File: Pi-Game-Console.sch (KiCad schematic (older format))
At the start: 115 parts, among them J1 Conn_01x02_Female, J10 Conn_01x04_Female, J2 FPC_Connector, J3 Conn_Coaxial, J5 Micro_SD_Card, J6 CAM1, J7 USB_A, J8 USB_A, J9 Conn_01x04_Female, SW1 SW_DIP_x01, SW10 Y_Button, SW11 D_PAD_UP_Button, SW12 D_PAD_DOWN_Button, SW13 D_PAD_LEFT_Button, SW14 D_PAD_RIGHT_Button, SW2 Home_Button, SW3 Start_Button, SW4 Select_Button, SW5 L_Button, SW6 R_Button, SW7 A_Button, SW8 B_Button, SW9 X_Button, U2 TDA2822, U3 FAN5333BSX, U4 AR1100, U5 ATmega32U4-AU, U6 FE1.1s, Y1 12MHz, Y2 16MHz, Y3 12MHz

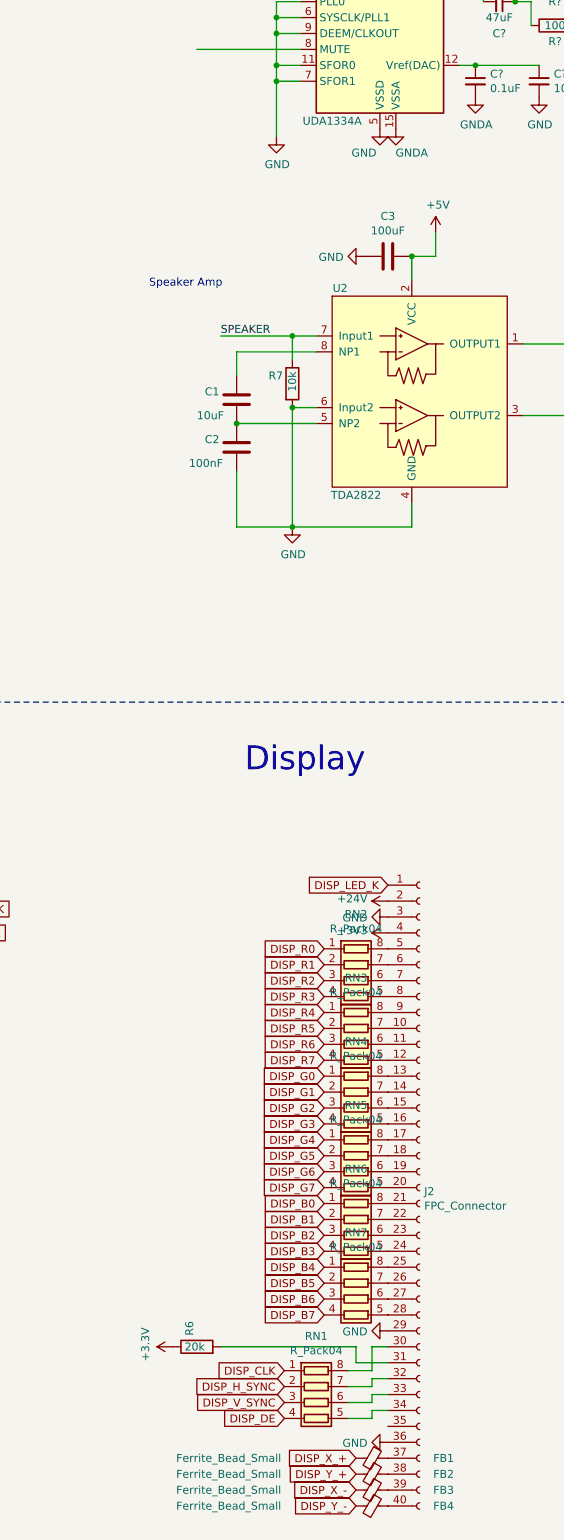
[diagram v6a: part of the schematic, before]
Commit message: Removed resistor arrays feeding into display
I really don't know that they're necessary, since the TFT friend from Adafruit doesn't have them, and they drive up the component count a fair amount.  Plus they're a real pain to solder.  If we change our mind later, they're easy to add back in.
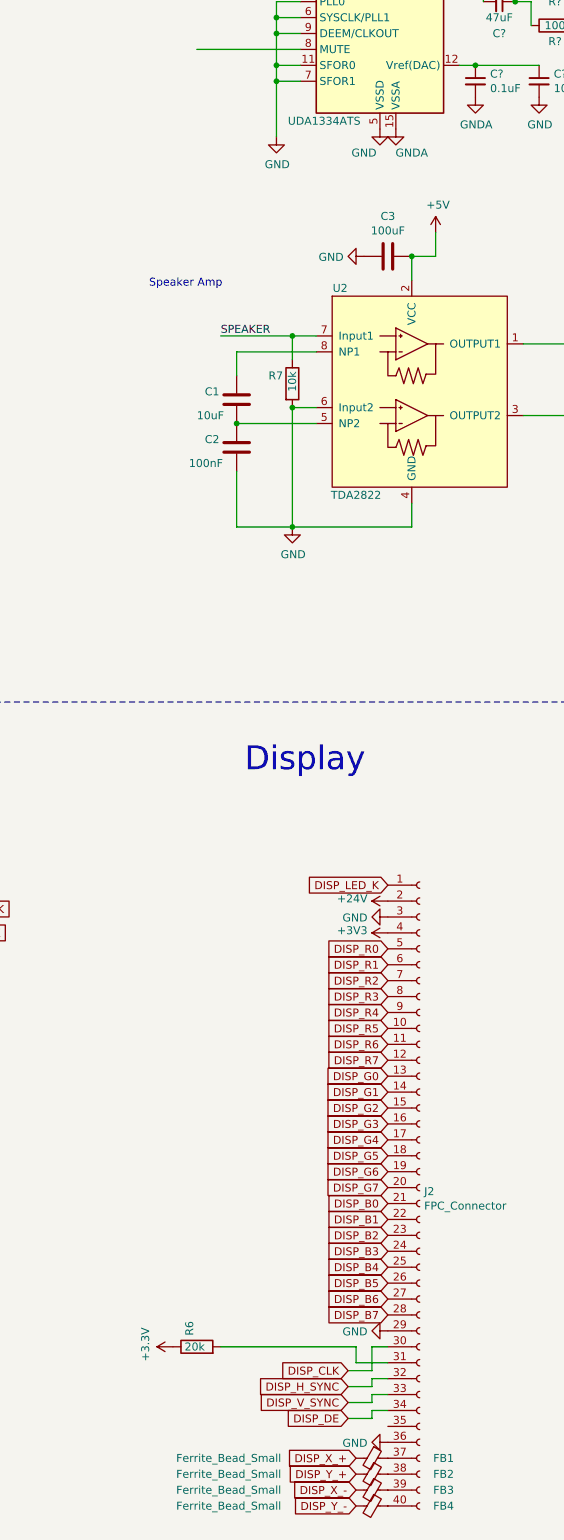
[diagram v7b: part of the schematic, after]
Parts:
- removed RN1, RN2, RN3, RN4, RN5, RN6, RN7: R_Pack04, symbol Device:R_Pack04
- U?: value UDA1334A -> UDA1334ATS
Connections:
- net DISP_B0: now also J2.21 (Pin_21)
- net DISP_B1: now also J2.22 (Pin_22)
- net DISP_B2: now also J2.23 (Pin_23)
- net DISP_B3: now also J2.24 (Pin_24)
- net DISP_B4: now also J2.25 (Pin_25)
- net DISP_B5: now also J2.26 (Pin_26)
- net DISP_B6: now also J2.27 (Pin_27)
- net DISP_B7: now also J2.28 (Pin_28)
- net DISP_CLK: now also J2.30 (Pin_30)
- net DISP_DE: now also J2.34 (Pin_34)
- net DISP_G0: now also J2.13 (Pin_13)
- net DISP_G1: now also J2.14 (Pin_14)
- net DISP_G2: now also J2.15 (Pin_15)
- net DISP_G3: now also J2.16 (Pin_16)
- net DISP_G4: now also J2.17 (Pin_17)
- net DISP_G5: now also J2.18 (Pin_18)
- net DISP_G6: now also J2.19 (Pin_19)
- net DISP_G7: now also J2.20 (Pin_20)
- net DISP_H_SYNC: now also J2.32 (Pin_32)
- net DISP_R0: now also J2.5 (Pin_5)
- net DISP_R1: now also J2.6 (Pin_6)
- net DISP_R2: now also J2.7 (Pin_7)
- net DISP_R3: now also J2.8 (Pin_8)
- net DISP_R4: now also J2.9 (Pin_9)
- net DISP_R5: now also J2.10 (Pin_10)
- net DISP_R6: now also J2.11 (Pin_11)
- net DISP_R7: now also J2.12 (Pin_12)
- net DISP_V_SYNC: now also J2.33 (Pin_33)
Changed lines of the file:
@@
 Wire Wire Line
 	20050 9150 19900 9150
-Text GLabel 6450 13350 0    50   Input ~ 0
+Text GLabel 6850 13350 0    50   Input ~ 0
 DISP_B2
-Text GLabel 6450 13450 0    50   Input ~ 0
+Text GLabel 6850 13450 0    50   Input ~ 0
 DISP_B3
-Text GLabel 6450 13550 0    50   Input ~ 0
+Text GLabel 6850 13550 0    50   Input ~ 0
 DISP_B4
-Text GLabel 6200 14300 0    50   Input ~ 0
+Text GLabel 6600 14300 0    50   Input ~ 0
 DISP_H_SYNC
-Text GLabel 6200 14400 0    50   Input ~ 0
+Text GLabel 6600 14400 0    50   Input ~ 0
 DISP_V_SYNC
-Text GLabel 6450 13650 0    50   Input ~ 0
+Text GLabel 6850 13650 0    50   Input ~ 0
 DISP_B5
-Text GLabel 6450 13750 0    50   Input ~ 0
+Text GLabel 6850 13750 0    50   Input ~ 0
 DISP_B6
-Text GLabel 6450 13850 0    50   Input ~ 0
+Text GLabel 6850 13850 0    50   Input ~ 0
 DISP_B7
-Text GLabel 6450 12750 0    50   Input ~ 0
+Text GLabel 6850 12750 0    50   Input ~ 0
 DISP_G4
-Text GLabel 6450 12850 0    50   Input ~ 0
+Text GLabel 6850 12850 0    50   Input ~ 0
 DISP_G5
-Text GLabel 6450 12950 0    50   Input ~ 0
+Text GLabel 6850 12950 0    50   Input ~ 0
 DISP_G6
-Text GLabel 6450 13050 0    50   Input ~ 0
+Text GLabel 6850 13050 0    50   Input ~ 0
 DISP_G7
-Text GLabel 6200 14200 0    50   Input ~ 0
+Text GLabel 6600 14200 0    50   Input ~ 0
 DISP_CLK
-Text GLabel 6200 14500 0    50   Input ~ 0
+Text GLabel 6600 14500 0    50   Input ~ 0
 DISP_DE
-Text GLabel 6450 13150 0    50   Input ~ 0
+Text GLabel 6850 13150 0    50   Input ~ 0
 DISP_B0
-Text GLabel 6450 13250 0    50   Input ~ 0
+Text GLabel 6850 13250 0    50   Input ~ 0
 DISP_B1
-Text GLabel 6450 12350 0    50   Input ~ 0
+Text GLabel 6850 12350 0    50   Input ~ 0
 DISP_G0
-Text GLabel 6450 11750 0    50   Input ~ 0
+Text GLabel 6850 11750 0    50   Input ~ 0
 DISP_R2
-Text GLabel 6450 11550 0    50   Input ~ 0
+Text GLabel 6850 11550 0    50   Input ~ 0
 DISP_R0
-Text GLabel 6450 11650 0    50   Input ~ 0
+Text GLabel 6850 11650 0    50   Input ~ 0
 DISP_R1
-Text GLabel 6450 11850 0    50   Input ~ 0
+Text GLabel 6850 11850 0    50   Input ~ 0
 DISP_R3
-Text GLabel 6450 11950 0    50   Input ~ 0
+Text GLabel 6850 11950 0    50   Input ~ 0
 DISP_R4
-Text GLabel 6450 12050 0    50   Input ~ 0
+Text GLabel 6850 12050 0    50   Input ~ 0
 DISP_R5
-Text GLabel 6450 12150 0    50   Input ~ 0
+Text GLabel 6850 12150 0    50   Input ~ 0
 DISP_R6
-Text GLabel 6450 12250 0    50   Input ~ 0
+Text GLabel 6850 12250 0    50   Input ~ 0
 DISP_R7
 $Comp
@@
 Wire Wire Line
 	10800 2750 10800 2450
-$Comp
-L Device:R_Pack04 RN2
-U 1 1 5E45DF44
-P 6650 11750
-F 0 "RN2" V 6233 11750 50  0000 C CNN
-F 1 "R_Pack04" V 6324 11750 50  0000 C CNN
-F 2 "" V 6925 11750 50  0001 C CNN
-F 3 "~" H 6650 11750 50  0001 C CNN
-	1    6650 11750
-	0    1    1    0
-$EndComp
-$Comp
-L Device:R_Pack04 RN3
-U 1 1 5E4602BE
-P 6650 12150
-F 0 "RN3" V 6233 12150 50  0000 C CNN
-F 1 "R_Pack04" V 6324 12150 50  0000 C CNN
-F 2 "" V 6925 12150 50  0001 C CNN
-F 3 "~" H 6650 12150 50  0001 C CNN
-	1    6650 12150
-	0    1    1    0
-$EndComp
-$Comp
-L Device:R_Pack04 RN6
-U 1 1 5E4620A6
-P 6650 13350
-F 0 "RN6" V 6233 13350 50  0000 C CNN
-F 1 "R_Pack04" V 6324 13350 50  0000 C CNN
-F 2 "" V 6925 13350 50  0001 C CNN
-F 3 "~" H 6650 13350 50  0001 C CNN
-	1    6650 13350
-	0    1    1    0
-$EndComp
-$Comp
-L Device:R_Pack04 RN7
-U 1 1 5E462A96
-P 6650 13750
-F 0 "RN7" V 6233 13750 50  0000 C CNN
-F 1 "R_Pack04" V 6324 13750 50  0000 C CNN
-F 2 "" V 6925 13750 50  0001 C CNN
-F 3 "~" H 6650 13750 50  0001 C CNN
-	1    6650 13750
-	0    1    1    0
-$EndComp
-$Comp
-L Device:R_Pack04 RN1
-U 1 1 5E4F56A2
-P 6400 14400
-F 0 "RN1" V 5983 14400 50  0000 C CNN
-F 1 "R_Pack04" V 6074 14400 50  0000 C CNN
-F 2 "" V 6675 14400 50  0001 C CNN
-F 3 "~" H 6400 14400 50  0001 C CNN
-	1    6400 14400
-	0    1    1    0
-$EndComp
 Wire Wire Line
 	6600 14300 6750 14300
@@
 	1    0    0    -1
 $EndComp
-$Comp
-L Device:R_Pack04 RN5
-U 1 1 5E4617F3
-P 6650 12950
-F 0 "RN5" V 6233 12950 50  0000 C CNN
-F 1 "R_Pack04" V 6324 12950 50  0000 C CNN
-F 2 "" V 6925 12950 50  0001 C CNN
-F 3 "~" H 6650 12950 50  0001 C CNN
-	1    6650 12950
-	0    1    1    0
-$EndComp
-$Comp
-L Device:R_Pack04 RN4
-U 1 1 5E460C5D
-P 6650 12550
-F 0 "RN4" V 6233 12550 50  0000 C CNN
-F 1 "R_Pack04" V 6324 12550 50  0000 C CNN
-F 2 "" V 6925 12550 50  0001 C CNN
-F 3 "~" H 6650 12550 50  0001 C CNN
-	1    6650 12550
-	0    1    1    0
-$EndComp
-Text GLabel 6450 12450 0    50   Input ~ 0
+Text GLabel 6850 12450 0    50   Input ~ 0
 DISP_G1
-Text GLabel 6450 12650 0    50   Input ~ 0
+Text GLabel 6850 12650 0    50   Input ~ 0
 DISP_G3
-Text GLabel 6450 12550 0    50   Input ~ 0
+Text GLabel 6850 12550 0    50   Input ~ 0
 DISP_G2
 $Comp
@@
 P 6800 5700
 F 0 "U?" H 6450 6350 50  0000 C CNN
-F 1 "UDA1334A" H 6500 5050 50  0000 C CNN
+F 1 "UDA1334ATS" H 6450 5050 50  0000 C CNN
 F 2 "Package_SO:SSOP-16_4.4x5.2mm_P0.65mm" H 6800 5700 50  0001 C CNN
 F 3 "http://www.nxp.com/docs/en/data-sheet/UDA1334ATS.pdf" H 6800 5700 50  0001 C CNN

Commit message: minor changes
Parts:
- C1, C2, C3: footprint (none) -> Capacitor_SMD:C_0805_2012Metric
- C10, C11, C4, C5, C6, C7, C8, C9: renamed from C?; footprint (none) -> Capacitor_SMD:C_0805_2012Metric
- C12: renamed from C6; footprint (none) -> Capacitor_SMD:C_0805_2012Metric
- C13: renamed from C9; footprint (none) -> Capacitor_SMD:C_0805_2012Metric
- C14: renamed from C10; footprint (none) -> Capacitor_SMD:C_0805_2012Metric
- C15: renamed from C11; footprint (none) -> Capacitor_SMD:C_0805_2012Metric
- C16: renamed from C12; footprint (none) -> Capacitor_SMD:C_0805_2012Metric
- C17: renamed from C13; footprint (none) -> Capacitor_SMD:C_0805_2012Metric
- C18: renamed from C14; footprint (none) -> Capacitor_SMD:C_0805_2012Metric
- C19: renamed from C15; footprint (none) -> Capacitor_SMD:C_0805_2012Metric
- C20: renamed from C16; footprint (none) -> Capacitor_SMD:C_0805_2012Metric
- C21: renamed from C17; footprint (none) -> Capacitor_SMD:C_0805_2012Metric
- C27: renamed from C23; value 10u -> 10uF
- C28: renamed from C24; value 10u -> 10uF
- C29: renamed from C25; value 10u -> 10uF
- D1, D3, D4: footprint (none) -> Diode_SMD:D_0805_2012Metric
- D2: footprint (none) -> LED_SMD:LED_0805_2012Metric
- FB1, FB6: renamed from FB?; footprint (none) -> Inductor_SMD:L_0805_2012Metric
- FB2: renamed from FB1; footprint (none) -> Inductor_SMD:L_0805_2012Metric
- FB3: renamed from FB2; footprint (none) -> Inductor_SMD:L_0805_2012Metric
- FB4: renamed from FB3; footprint (none) -> Inductor_SMD:L_0805_2012Metric
- FB5: renamed from FB4; footprint (none) -> Inductor_SMD:L_0805_2012Metric
- J4: renamed from J?; footprint (none) -> Connector_Audio:Jack_3.5mm_PJ311_Horizontal
- JP1, JP2, JP3: footprint (none) -> Jumper:SolderJumper-2_P1.3mm_Open_TrianglePad1.0x1.5mm
- L1: footprint (none) -> Inductor_SMD:L_Bourns-SRU1028_10.0x10.0mm
- R1, R12, R13, R14, R6, R7: footprint (none) -> Resistor_SMD:R_0805_2012Metric
- R10, R11, R8, R9: renamed from R?; footprint (none) -> Resistor_SMD:R_0805_2012Metric
- R15: renamed from R17; footprint (none) -> Resistor_SMD:R_0805_2012Metric
- R16: renamed from R18; footprint (none) -> Resistor_SMD:R_0805_2012Metric
- R17: renamed from R19; footprint (none) -> Resistor_SMD:R_0805_2012Metric
- R18: renamed from R20; footprint (none) -> Resistor_SMD:R_0805_2012Metric
- R19: renamed from R21; footprint (none) -> Resistor_SMD:R_0805_2012Metric
- R20: renamed from R22; footprint (none) -> Resistor_SMD:R_0805_2012Metric
- RV1: footprint (none) -> Potentiometer_SMD:Potentiometer_Bourns_3214G_Horizontal
- TP1, TP2, TP3, TP4, TP5: footprint (none) -> TestPoint:TestPoint_Pad_D1.5mm
- U2: footprint (none) -> Package_SO:SOIC-8_3.9x4.9mm_P1.27mm
- U3: footprint (none) -> Package_SO:SO-5_4.4x3.6mm_P1.27mm
- U4: footprint (none) -> Package_SO:SOIC-20W_7.5x12.8mm_P1.27mm
- gave numbers to parts that had none: 1
- renumbered C18 to C22, C19 to C23, C20 to C24, C21 to C25, C22 to C26, R23 to R21, R24 to R22, R25 to R23
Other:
- note added: "Second Speaker Out?"
